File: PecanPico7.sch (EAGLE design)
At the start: 178 parts, among them IC1 Si4060-B1B-FM, IC10 TPS62260DRVT, IC11 TPS62261DRVT, IC12 TPS63021, IC13 RF6886, IC14 TPS78227DDCR, IC16 PAC1720-1-AIA-TR, IC2 Si4060-B1B-FM, IC3 BME280_BME280, IC4 uBlox MAX7/8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

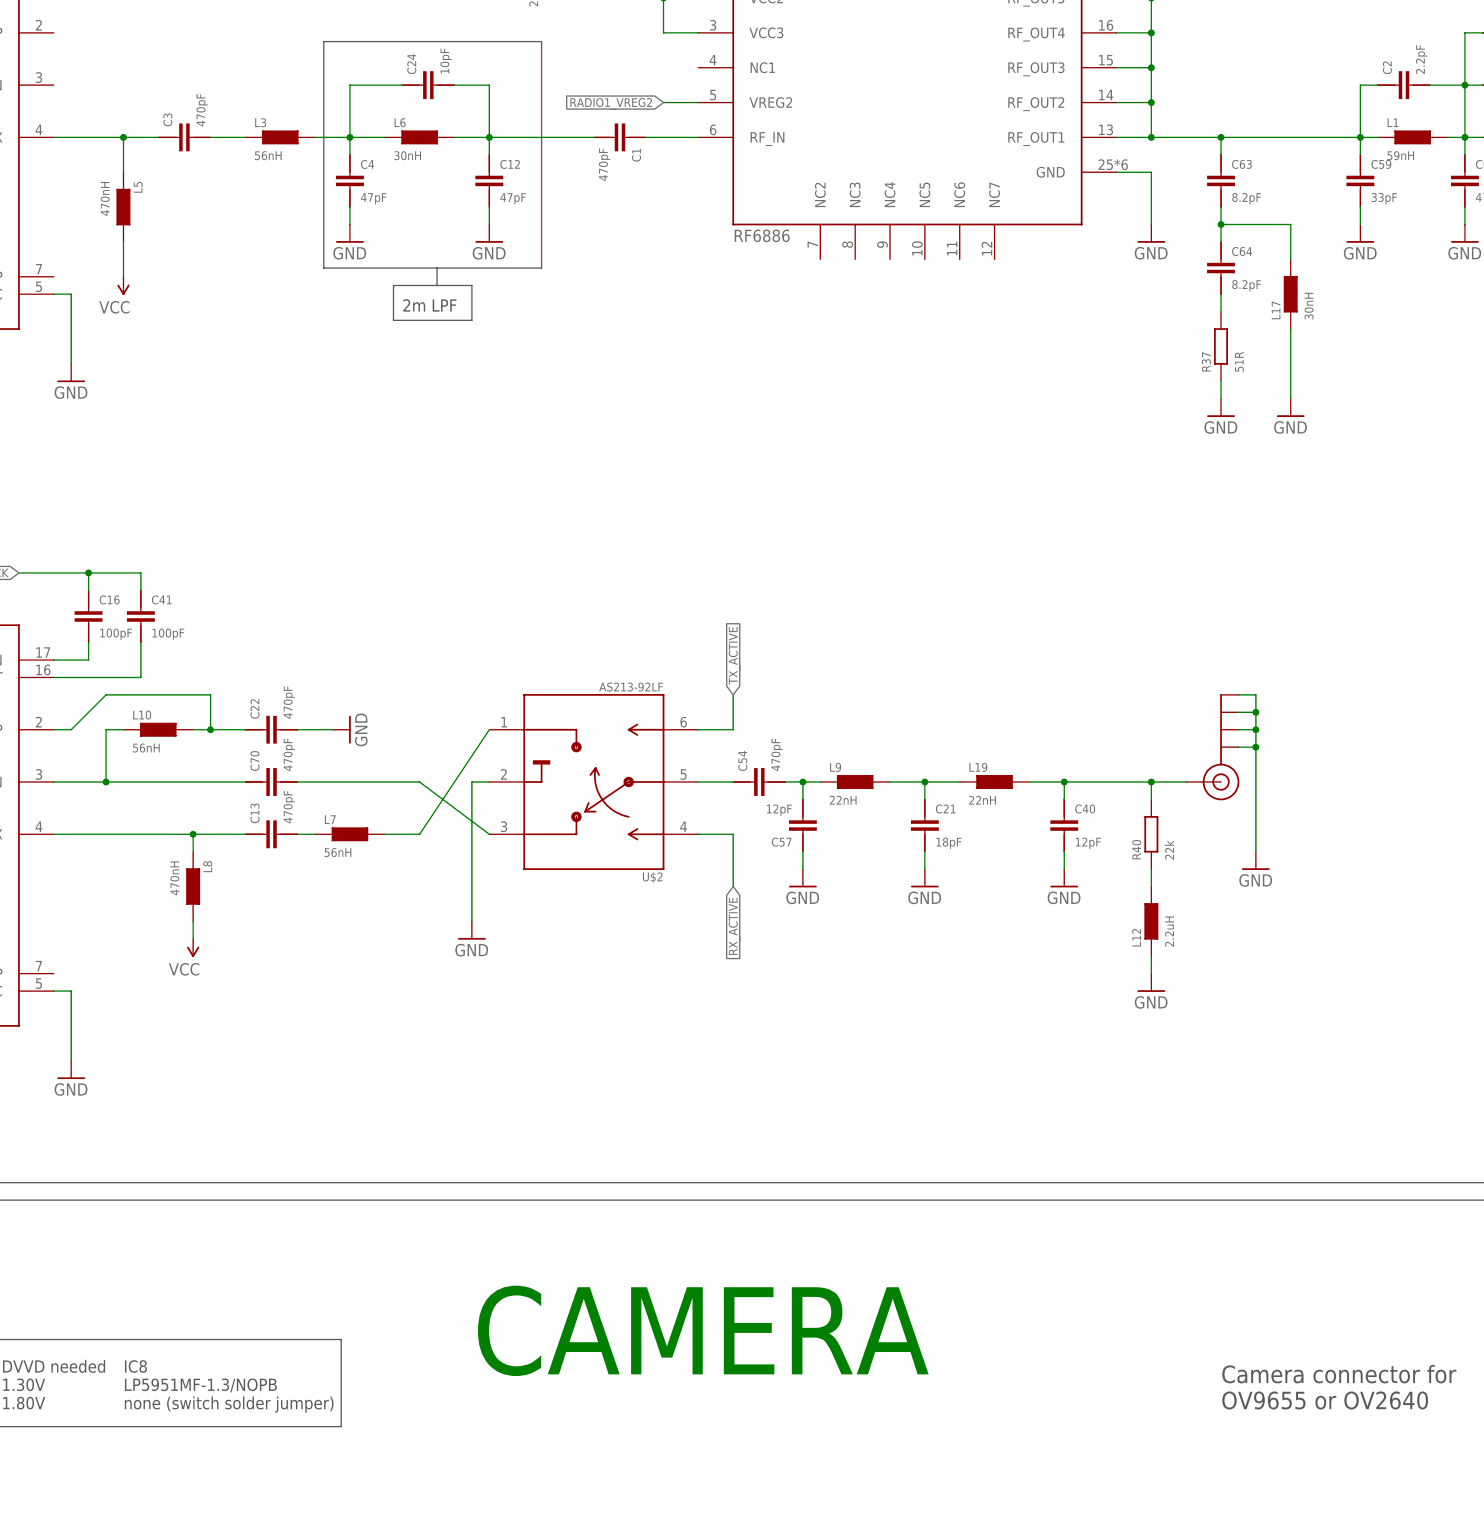
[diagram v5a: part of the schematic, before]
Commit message: Added decoupling capacitor
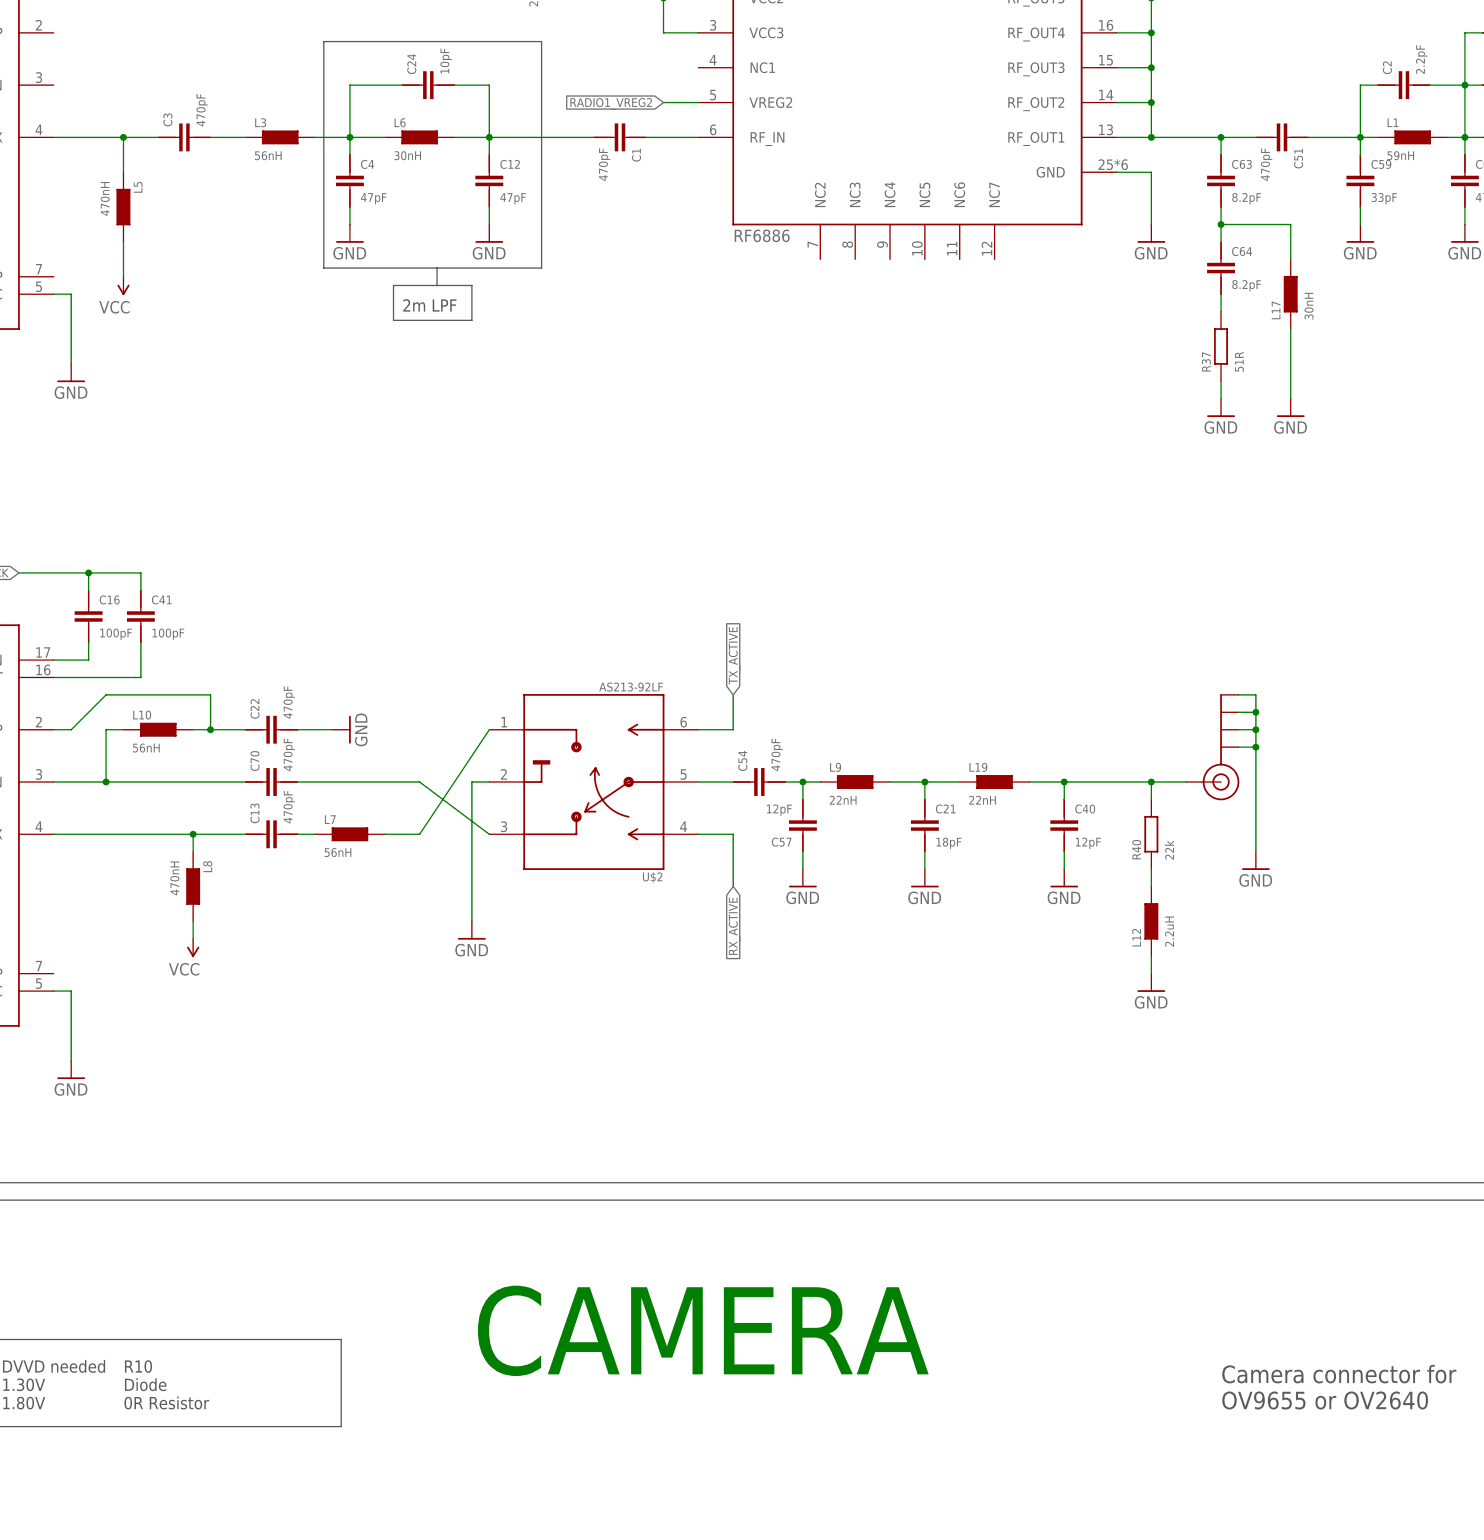
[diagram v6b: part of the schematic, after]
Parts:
- added C51: 470pF, PecanPico6:CAP-0402
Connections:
- new net N$8: C2.2, C51.2, C59.2, L1.1
- net N$43: now also C51.1; no longer C2.2, C59.2, L1.1
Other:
- note added: "R10 Diode 0R Resistor"
- note removed: "IC8 LP5951MF-1.3/NOPB none (switch solder jumper)"
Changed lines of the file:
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@@
 <part name="R10" library="PecanPico6" deviceset="RES-0402" device="" value="DIODE"/>
 <part name="R22" library="PecanPico6" deviceset="RES-0402" device="" value="10k"/>
+<part name="C51" library="PecanPico6" deviceset="CAP-0402" device="" value="470pF"/>
 </parts>
 <sheets>
@@
 1.30V
 1.80V</text>
-<text x="152.4" y="218.44" size="1.778" layer="97">IC8
-LP5951MF-1.3/NOPB
-none (switch solder jumper)</text>
+<text x="152.4" y="218.44" size="1.778" layer="97">R10
+Diode
+0R Resistor</text>
 <wire x1="119.38" y1="228.6" x2="184.15" y2="228.6" width="0.1524" layer="97"/>
 <wire x1="184.15" y1="228.6" x2="184.15" y2="215.9" width="0.1524" layer="97"/>
@@
 <instance part="R10" gate="G$1" x="279.4" y="170.18"/>
 <instance part="R22" gate="G$1" x="-132.08" y="81.28"/>
+<instance part="C51" gate="G$1" x="322.58" y="403.86" rot="R270"/>
 </instances>
 <busses>
@@
 <wire x1="302.26" y1="403.86" x2="312.42" y2="403.86" width="0.1524" layer="91"/>
 <junction x="302.26" y="403.86"/>
-<wire x1="312.42" y1="403.86" x2="332.74" y2="403.86" width="0.1524" layer="91"/>
 <wire x1="302.26" y1="429.26" x2="302.26" y2="434.34" width="0.1524" layer="91"/>
 <junction x="302.26" y="429.26"/>
 <pinref part="L11" gate="G$1" pin="1"/>
-<pinref part="C59" gate="G$1" pin="2"/>
-<wire x1="332.74" y1="403.86" x2="335.28" y2="403.86" width="0.1524" layer="91"/>
-<wire x1="332.74" y1="401.32" x2="332.74" y2="403.86" width="0.1524" layer="91"/>
-<pinref part="L1" gate="G$1" pin="1"/>
-<junction x="332.74" y="403.86"/>
-<wire x1="332.74" y1="403.86" x2="332.74" y2="411.48" width="0.1524" layer="91"/>
-<pinref part="C2" gate="G$1" pin="2"/>
-<wire x1="332.74" y1="411.48" x2="335.28" y2="411.48" width="0.1524" layer="91"/>
 <wire x1="312.42" y1="403.86" x2="312.42" y2="401.32" width="0.1524" layer="91"/>
-<junction x="312.42" y="403.86"/>
 <pinref part="C63" gate="G$1" pin="2"/>
+<pinref part="C51" gate="G$1" pin="1"/>
+<wire x1="312.42" y1="403.86" x2="317.5" y2="403.86" width="0.1524" layer="91"/>
+<junction x="312.42" y="403.86"/>
 </segment>
 </net>
@@
 </segment>
 </net>
+<net name="N$8" class="0">
+<segment>
+<pinref part="C2" gate="G$1" pin="2"/>
+<wire x1="332.74" y1="411.48" x2="335.28" y2="411.48" width="0.1524" layer="91"/>
+<pinref part="L1" gate="G$1" pin="1"/>
+<wire x1="332.74" y1="403.86" x2="335.28" y2="403.86" width="0.1524" layer="91"/>
+<junction x="332.74" y="403.86"/>
+<wire x1="332.74" y1="403.86" x2="332.74" y2="411.48" width="0.1524" layer="91"/>
+<pinref part="C59" gate="G$1" pin="2"/>
+<wire x1="332.74" y1="401.32" x2="332.74" y2="403.86" width="0.1524" layer="91"/>
+<pinref part="C51" gate="G$1" pin="2"/>
+<wire x1="325.12" y1="403.86" x2="332.74" y2="403.86" width="0.1524" layer="91"/>
+</segment>
+</net>

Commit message: Connected LED4 to MCU pin, added GND cutout
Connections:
- new net LED4: IC5G$2.PF7, R34.2
- net GND: no longer IC6.GND5, IC6.GND6, R34.2
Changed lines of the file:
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@@
 <part name="R34" library="PecanPico6" deviceset="RES-0402" device="" value="1k"/>
 <part name="P+38" library="PecanPico6" deviceset="3.3V" device="" value="VCC"/>
-<part name="GND95" library="PecanPico6" deviceset="GND" device=""/>
 <part name="IC6" library="stm32f42x" deviceset="ALM-GP003" device=""/>
 <part name="GND94" library="PecanPico6" deviceset="GND" device=""/>
@@
 <instance part="R34" gate="G$1" x="261.62" y="586.74"/>
 <instance part="P+38" gate="G$1" x="243.84" y="622.3"/>
-<instance part="GND95" gate="1" x="271.78" y="586.74" rot="R90"/>
 <instance part="IC6" gate="G$1" x="-226.06" y="304.8"/>
-<instance part="GND94" gate="1" x="-223.52" y="276.86"/>
+<instance part="GND94" gate="1" x="-228.6" y="276.86"/>
 <instance part="L2" gate="G$1" x="-223.52" y="332.74" rot="R90"/>
 <instance part="L15" gate="G$1" x="-223.52" y="347.98" rot="R90"/>
@@
 </segment>
 <segment>
-<pinref part="R34" gate="G$1" pin="2"/>
-<wire x1="266.7" y1="586.74" x2="269.24" y2="586.74" width="0.1524" layer="91"/>
-<pinref part="GND95" gate="1" pin="GND"/>
-</segment>
-<segment>
-<pinref part="IC6" gate="G$1" pin="GND6"/>
-<wire x1="-223.52" y1="287.02" x2="-223.52" y2="284.48" width="0.1524" layer="91"/>
-<pinref part="IC6" gate="G$1" pin="GND5"/>
-<wire x1="-226.06" y1="287.02" x2="-226.06" y2="284.48" width="0.1524" layer="91"/>
-<wire x1="-226.06" y1="284.48" x2="-223.52" y2="284.48" width="0.1524" layer="91"/>
 <pinref part="IC6" gate="G$1" pin="GND4"/>
 <wire x1="-228.6" y1="287.02" x2="-228.6" y2="284.48" width="0.1524" layer="91"/>
-<wire x1="-228.6" y1="284.48" x2="-226.06" y2="284.48" width="0.1524" layer="91"/>
-<junction x="-226.06" y="284.48"/>
 <pinref part="IC6" gate="G$1" pin="GND3"/>
 <wire x1="-231.14" y1="287.02" x2="-231.14" y2="284.48" width="0.1524" layer="91"/>
@@
 <wire x1="-236.22" y1="284.48" x2="-233.68" y2="284.48" width="0.1524" layer="91"/>
 <junction x="-233.68" y="284.48"/>
-<wire x1="-223.52" y1="284.48" x2="-223.52" y2="279.4" width="0.1524" layer="91"/>
-<junction x="-223.52" y="284.48"/>
+<wire x1="-228.6" y1="284.48" x2="-228.6" y2="279.4" width="0.1524" layer="91"/>
 <pinref part="GND94" gate="1" pin="GND"/>
 </segment>
@@
 </segment>
 </net>
+<net name="LED4" class="0">
+<segment>
+<pinref part="R34" gate="G$1" pin="2"/>
+<wire x1="266.7" y1="586.74" x2="269.24" y2="586.74" width="0.1524" layer="91"/>
+<label x="269.24" y="586.74" size="1.27" layer="95" xref="yes"/>
+</segment>
+<segment>
+<pinref part="IC5" gate="G$2" pin="PF7"/>
+<wire x1="-180.34" y1="60.96" x2="-185.42" y2="60.96" width="0.1524" layer="91"/>
+<label x="-185.42" y="60.96" size="1.27" layer="95" rot="R180" xref="yes"/>
+</segment>
+</net>

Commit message: Done many things Added mounting point for camera Replaced 1X4 pin header with 2X4 pinheader (I2C header) Added battery and solar jumper Added voltage divider for Vsolar Removed 100mil mounting point
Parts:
- removed JP1: (no value), SparkFun-Connectors:M04PTH
- added R23, R25: 1k, PecanPico6:RES-0402
- JP4: device SparkFun-Connectors:M01PTH -> SparkFun-Connectors:M04X2SMD
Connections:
- removed net N$14: BATT.+, SJ3.1
- new net BATTERY: BATT.+, JP4.8, SJ3.1
- new net VSOLAR_DIFF: IC5G$1.PC4, R23.1, R25.2
- net GND: now also JP4.3, JP4.4, R25.1; no longer JP1.2, JP4.1
- net I2C_SCL: now also JP4.5; no longer JP1.3
- net I2C_SDA: now also JP4.7; no longer JP1.4
- net VBAT: now also JP4.6
- net VCC: now also JP4.1; no longer JP1.1
- net VSOLAR: now also JP4.2, R23.2; no longer IC5G$1.PC4
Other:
- moved on the sheet: BATT, C15, C46, JP2, JP5, JP6
